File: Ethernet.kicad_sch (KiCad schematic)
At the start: 1 part, among them U12 SI-51005-F

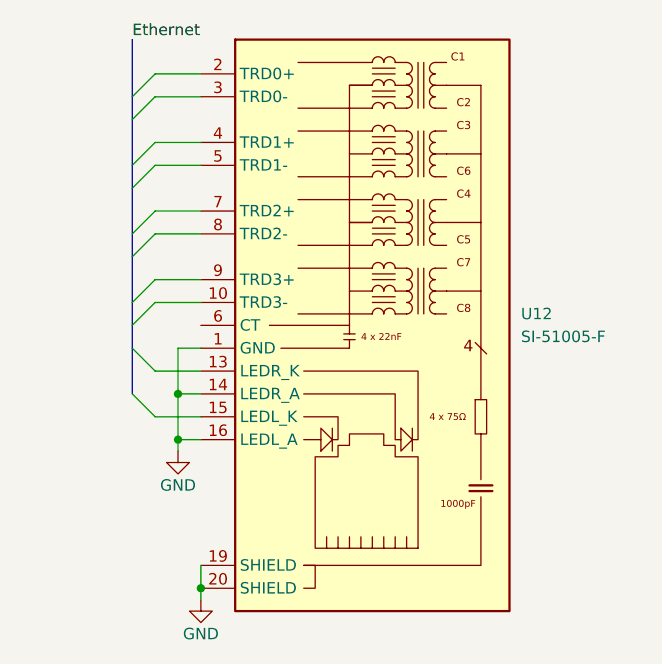
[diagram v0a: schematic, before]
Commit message: Cleaned up schematics and added gnds and no-connects
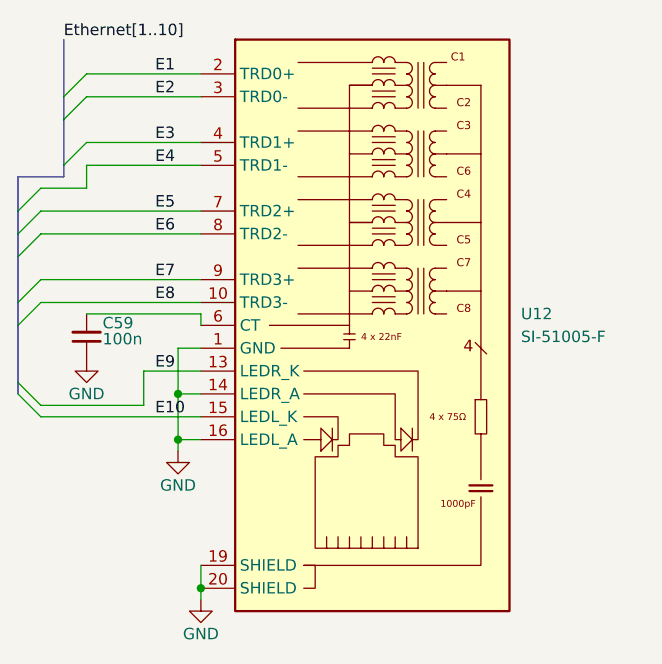
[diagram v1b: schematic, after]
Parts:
- added C59: 100n, symbol Device:C_Small
- U12: footprint (none) -> Ethernet_con:TE_RJ45-8L-B
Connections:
- net GND: now also C59.1
- net E8: now reaches U12.10 (TRD3-)
- net E9: now reaches U12.13 (LEDR_K)
- net E10: now reaches U12.15 (LEDL_K)
- net E1: now reaches U12.2 (TRD0+)
- net E2: now reaches U12.3 (TRD0-)
- net E3: now reaches U12.4 (TRD1+)
- net E4: now reaches U12.5 (TRD1-)
- net at U12.6 (CT): now also C59.2
- net E5: now reaches U12.7 (TRD2+)
- net E6: now reaches U12.8 (TRD2-)
- net E7: now reaches U12.9 (TRD3+)
